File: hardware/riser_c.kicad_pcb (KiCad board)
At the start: 2 copper layers, 46.5 x 63.5 mm, 1 part

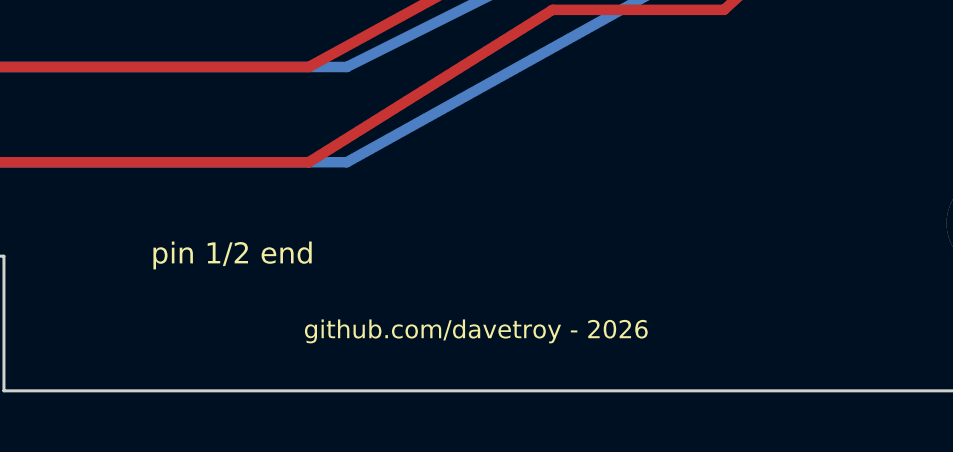
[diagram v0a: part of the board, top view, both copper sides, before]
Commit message: Order prep: memorial notice on both boards, ORDER.md package
Both boards now carry "(c) 2026 David Troy, in memory of Stephen
Troy." on the silkscreen — the card along its bottom edge, the riser
on two lines. Regenerated boards, fab zips, gerbers, and 1:1 plots;
re-verified DRC-clean (0 violations, 0 unconnected on both). ORDER.md
carries the full PCBWay parameter set, the pre-upload checklist, the
per-card BOM, and the bring-up sequence for when the boards arrive.

Co-Authored-By: Claude Fable 5 <noreply@anthropic.com>
Claude-Session: https://claude.ai/code/session_01PB6zhL6oFB9zbtD4W85UDt
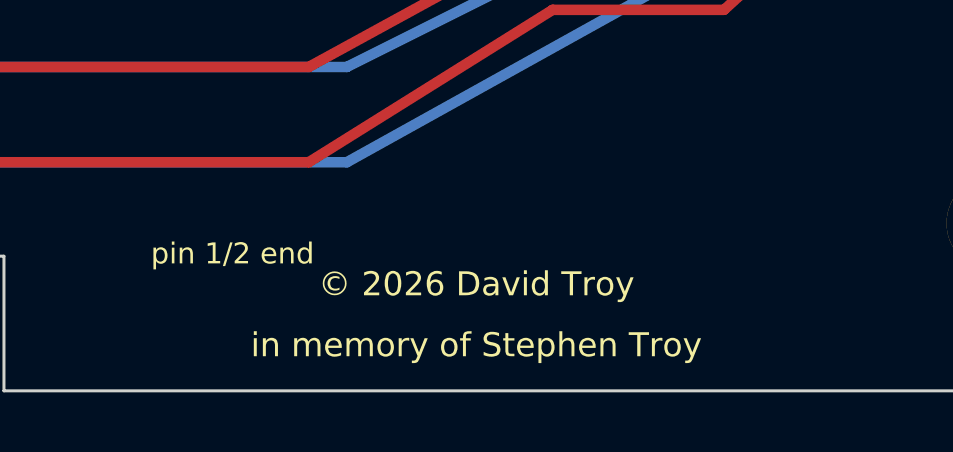
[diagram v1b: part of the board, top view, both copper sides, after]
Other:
- board text added: "in memory of Stephen Troy"
- board text added: "© 2026 David Troy"
- board text removed: "github.com/davetroy - 2026"
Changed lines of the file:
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@@
   (gr_text "pin 1/2 end" (at 137.6200 143.9280) (layer "F.SilkS") (effects (font (size 0.7 0.7) (thickness 0.15))))
   (gr_text "pin 29/30 end" (at 137.6200 98.2080) (layer "F.SilkS") (effects (font (size 0.7 0.7) (thickness 0.15))))
-  (gr_text "github.com/davetroy - 2026" (at 145.7480 146.4680) (layer "F.SilkS") (effects (font (size 0.6 0.6) (thickness 0.15))))
+  (gr_text "© 2026 David Troy" (at 145.7480 144.9440) (layer "F.SilkS") (effects (font (size 0.8 0.8) (thickness 0.15))))
+  (gr_text "in memory of Stephen Troy" (at 145.7480 146.9760) (layer "F.SilkS") (effects (font (size 0.8 0.8) (thickness 0.15))))
   (segment (start 129.4920 140.8800) (end 140.1600 140.8800) (width 0.35) (layer "F.Cu") (net 2))
   (segment (start 140.1600 140.8800) (end 148.2880 135.8000) (width 0.35) (layer "F.Cu") (net 2))
